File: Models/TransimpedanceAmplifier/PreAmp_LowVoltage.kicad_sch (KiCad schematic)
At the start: 6 parts, among them U7 LM78L05, 5V, 5%, U9 LM79L05, -5V, 5%

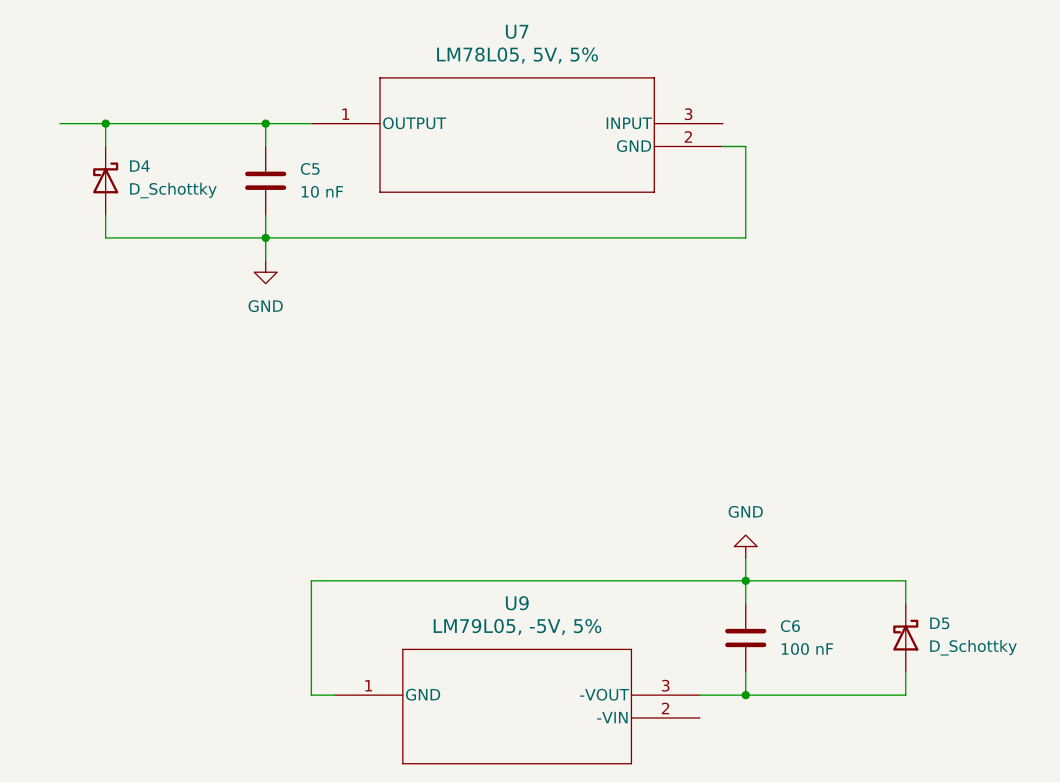
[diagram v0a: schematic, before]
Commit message: Labeled all the input/output nodes of the power subsystems
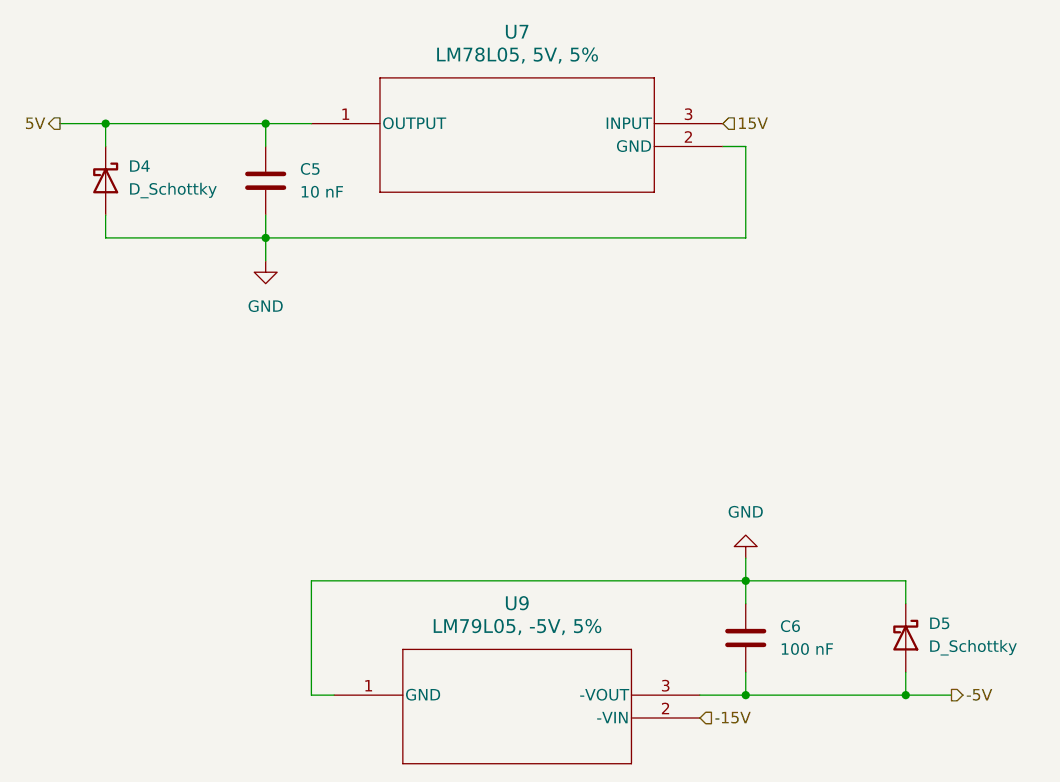
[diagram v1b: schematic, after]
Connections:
- net -15V: now reaches U9.2 (-VIN)
- net -5V: now reaches C6.2, D5.2 (A), U9.3 (-VOUT)
- net 5V: now reaches C5.1, D4.1 (K), U7.1 (OUTPUT)
- net 15V: now reaches U7.3 (INPUT)
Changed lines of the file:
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@@
 	(paper "A4")
 	(junction
+		(at 185.42 119.38)
+		(diameter 0)
+		(color 0 0 0 0)
+	)
+	(junction
 		(at 167.64 106.68)
 		(diameter 0)
@@
 	(wire
 		(pts
+			(xy 185.42 119.38) (xy 190.5 119.38)
+		)
+		(stroke
+			(width 0)
+			(type default)
+		)
+	)
+	(wire
+		(pts
 			(xy 162.56 119.38) (xy 167.64 119.38)
 		)
@@
 		)
 	)
+	(hierarchical_label "5V"
+		(shape output)
+		(at 91.44 55.88 180)
+		(effects
+			(font
+				(size 1.27 1.27)
+			)
+			(justify right)
+		)
+	)
+	(hierarchical_label "-15V"
+		(shape input)
+		(at 162.56 121.92 0)
+		(effects
+			(font
+				(size 1.27 1.27)
+			)
+			(justify left)
+		)
+	)
+	(hierarchical_label "-5V"
+		(shape output)
+		(at 190.5 119.38 0)
+		(effects
+			(font
+				(size 1.27 1.27)
+			)
+			(justify left)
+		)
+	)
+	(hierarchical_label "15V"
+		(shape input)
+		(at 165.1 55.88 0)
+		(effects
+			(font
+				(size 1.27 1.27)
+			)
+			(justify left)
+		)
+	)
